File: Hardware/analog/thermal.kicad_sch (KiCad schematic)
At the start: 11 parts, among them M501 Fan_4pin, Q501 MMBT3904, Q502 PN2222A, U501 EMC2101-R

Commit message: More tweaks to load board
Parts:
- added J501, J502: Conn_01x01, programmable-load:MillMax-2108-2, symbol Connector_Generic:Conn_01x01
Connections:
- net TEMP_DN: now also J502.1 (Pin_1)
- net TEMP_DP: now also J501.1 (Pin_1)
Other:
- moved on the sheet: Q502
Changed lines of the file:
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@@
   (junction (at 214.63 102.87) (diameter 0) (color 0 0 0 0)
   )
-  (junction (at 259.08 30.48) (diameter 0) (color 0 0 0 0)
-  )
   (junction (at 228.6 97.79) (diameter 0) (color 0 0 0 0)
   )
+  (junction (at 259.08 27.94) (diameter 0) (color 0 0 0 0)
+  )
   (junction (at 236.22 105.41) (diameter 0) (color 0 0 0 0)
   )
@@
     (stroke (width 0) (type default) (color 0 0 0 0))
   )
+  (wire (pts (xy 259.08 22.86) (xy 259.08 27.94))
+    (stroke (width 0) (type default) (color 0 0 0 0))
+  )
+  (wire (pts (xy 266.7 33.02) (xy 266.7 35.56))
+    (stroke (width 0) (type default) (color 0 0 0 0))
+  )
   (wire (pts (xy 196.85 38.1) (xy 198.12 38.1))
     (stroke (width 0) (type default) (color 0 0 0 0))
@@
     (stroke (width 0) (type default) (color 0 0 0 0))
   )
-  (wire (pts (xy 249.555 30.48) (xy 259.08 30.48))
+  (wire (pts (xy 249.555 27.94) (xy 259.08 27.94))
     (stroke (width 0) (type default) (color 0 0 0 0))
   )
@@
     (stroke (width 0) (type default) (color 0 0 0 0))
   )
-  (wire (pts (xy 259.08 25.4) (xy 259.08 30.48))
-    (stroke (width 0) (type default) (color 0 0 0 0))
-  )
-  (wire (pts (xy 266.7 25.4) (xy 259.08 25.4))
+  (wire (pts (xy 266.7 22.86) (xy 259.08 22.86))
     (stroke (width 0) (type default) (color 0 0 0 0))
   )
@@
   )
   (text "Place Q502 on/near heatsink,\nconnected via twisted pair wire\nUsed for hardware fan control"
-    (at 278.13 42.545 0)
+    (at 272.415 44.45 0)
     (effects (font (size 1.27 1.27)) (justify right bottom))
   )
@@
     (effects (font (size 1.27 1.27)) (justify left bottom))
   )
-  (label "TEMP_DP" (at 249.555 30.48 0)
+  (label "TEMP_DP" (at 249.555 27.94 0)
     (effects (font (size 1.27 1.27)) (justify left bottom))
   )
@@
     (pin "2")
   )
+  (symbol (lib_id "Connector_Generic:Conn_01x01") (at 244.475 27.94 0) (mirror y) (unit 1)
+    (in_bom yes) (on_board yes)
+    (property "Reference" "J501" (id 0) (at 244.475 24.13 0))
+    (property "Value" "Conn_01x01" (id 1) (at 244.475 24.13 0)
+      (effects (font (size 1.27 1.27)) hide)
+    )
+    (property "Footprint" "programmable-load:MillMax-2108-2" (id 2) (at 244.475 27.94 0)
+      (effects (font (size 1.27 1.27)) hide)
+    )
+    (property "Datasheet" "~" (id 3) (at 244.475 27.94 0)
+      (effects (font (size 1.27 1.27)) hide)
+    )
+    (property "MPN" "2108-2-00-01-00-00-07-0" (id 4) (at 244.475 27.94 0)
+      (effects (font (size 1.27 1.27)) hide)
+    )
+    (pin "1")
+  )
   (symbol (lib_id "Device:R_Small") (at 209.55 91.44 0) (mirror x) (unit 1)
     (in_bom yes) (on_board yes) (fields_autoplaced)
@@
     (pin "1")
   )
+  (symbol (lib_id "Connector_Generic:Conn_01x01") (at 244.475 35.56 0) (mirror y) (unit 1)
+    (in_bom yes) (on_board yes)
+    (property "Reference" "J502" (id 0) (at 244.475 31.75 0))
+    (property "Value" "Conn_01x01" (id 1) (at 244.475 31.75 0)
+      (effects (font (size 1.27 1.27)) hide)
+    )
+    (property "Footprint" "programmable-load:MillMax-2108-2" (id 2) (at 244.475 35.56 0)
+      (effects (font (size 1.27 1.27)) hide)
+    )
+    (property "Datasheet" "~" (id 3) (at 244.475 35.56 0)
+      (effects (font (size 1.27 1.27)) hide)
+    )
+    (property "MPN" "2108-2-00-01-00-00-07-0" (id 4) (at 244.475 35.56 0)
+      (effects (font (size 1.27 1.27)) hide)
+    )
+    (pin "1")
+  )
   (symbol (lib_id "Device:C_Polarized_Small") (at 252.73 99.06 0) (unit 1)
     (in_bom yes) (on_board yes) (fields_autoplaced)
@@
     (pin "4")
   )
-  (symbol (lib_id "Transistor_BJT:PN2222A") (at 264.16 30.48 0) (unit 1)
+  (symbol (lib_id "Transistor_BJT:PN2222A") (at 264.16 27.94 0) (unit 1)
     (in_bom yes) (on_board no) (fields_autoplaced)
-    (property "Reference" "Q502" (id 0) (at 269.875 29.2099 0)
-      (effects (font (size 1.27 1.27)) (justify left))
-    )
-    (property "Value" "PN2222A" (id 1) (at 269.875 31.7499 0)
-      (effects (font (size 1.27 1.27)) (justify left))
-    )
-    (property "Footprint" "Package_TO_SOT_THT:TO-92_Inline" (id 2) (at 269.24 32.385 0)
+    (property "Reference" "Q502" (id 0) (at 269.875 26.6699 0)
+      (effects (font (size 1.27 1.27)) (justify left))
+    )
+    (property "Value" "PN2222A" (id 1) (at 269.875 29.2099 0)
+      (effects (font (size 1.27 1.27)) (justify left))
+    )
+    (property "Footprint" "Package_TO_SOT_THT:TO-92_Inline" (id 2) (at 269.24 29.845 0)
       (effects (font (size 1.27 1.27) italic) (justify left) hide)
     )
-    (property "Datasheet" "https://www.onsemi.com/pub/Collateral/PN2222-D.PDF" (id 3) (at 264.16 30.48 0)
+    (property "Datasheet" "https://www.onsemi.com/pub/Collateral/PN2222-D.PDF" (id 3) (at 264.16 27.94 0)
       (effects (font (size 1.27 1.27)) (justify left) hide)
     )
-    (property "MPN" "PN2222ATA" (id 4) (at 264.16 30.48 0)
-      (effects (font (size 1.27 1.27)) hide)
-    )
+    (property "MPN" "PN2222ATA" (id 4) (at 264.16 27.94 0)
+      (effects (font (size 1.27 1.27)) hide)
+    )

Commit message: Initial pass at analog board
- Everything currently in the schematic is routed, and stuff is
  reasonably sanely laid out

- Some compromises: namely, the zero offset doesn't use the DAC
  reference for its positive, but generates a separate 2.5V via the
  shunt diodes; this is then shared between both op-amps. That avoids
  the DAC/ADC reference getting noisified

  Also, we don't have an ADC for measuring the temperature sensors yet,
  and in fact, those aren't routed out (or existent really) yet either

- TODO: add test points for drive voltages and current sense voltages
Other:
- title: (none) -> 300W Analog Load Board
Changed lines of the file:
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@@
 (kicad_sch (version 20211123) (generator eeschema)
   (paper "A4")
+  (title_block
+    (title "300W Analog Load Board")
+    (rev "1")
+  )
   (junction (at 214.63 102.87) (diameter 0) (color 0 0 0 0)
   )

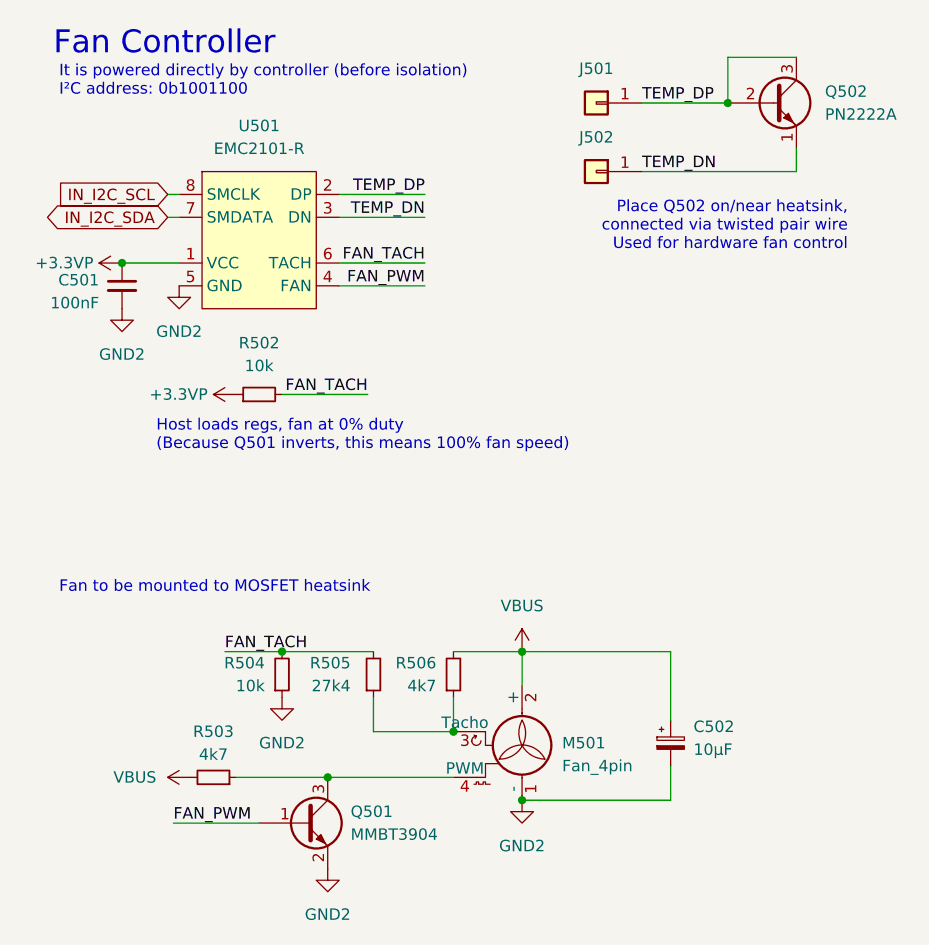
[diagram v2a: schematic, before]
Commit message: Added more decoupling for reference
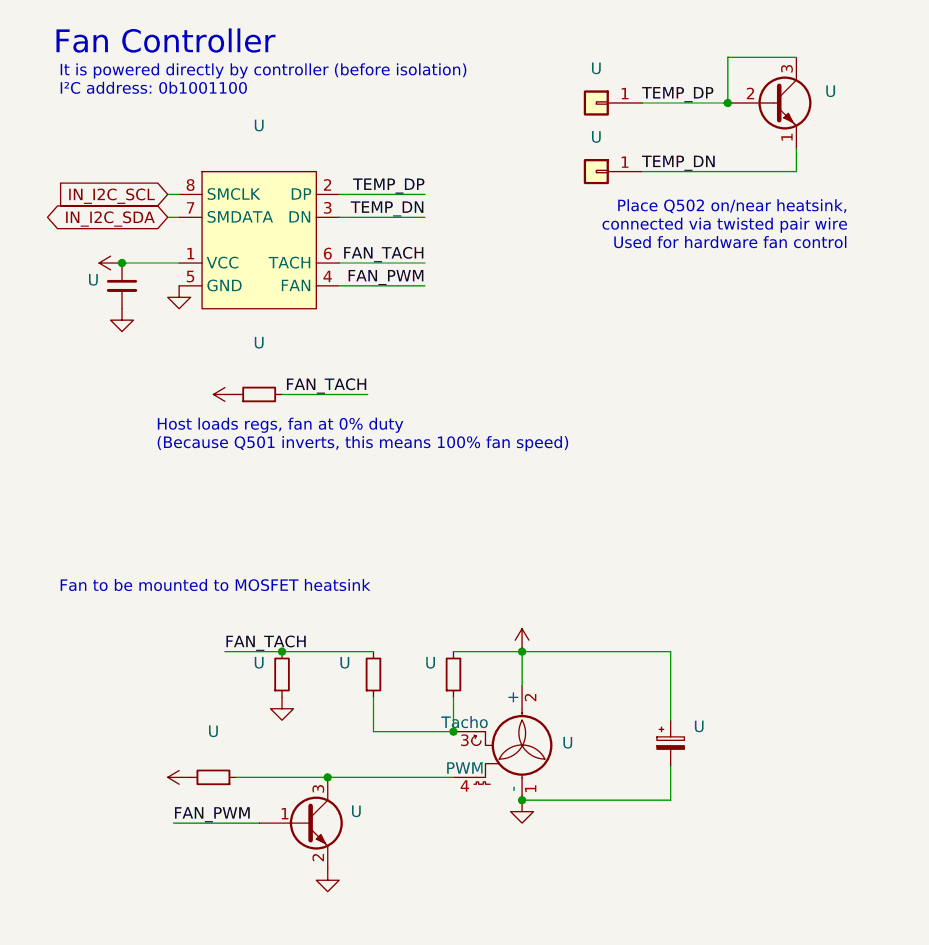
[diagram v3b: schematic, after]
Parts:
- U: renamed from U501; value EMC2101-R -> (none); footprint Package_SO:MSOP-8_3x3mm_P0.65mm -> (none)
- U: renamed from R506; value 4k7 -> (none); footprint Resistor_SMD:R_0805_2012Metric_Pad1.20x1.40mm_HandSolder -> (none)
- U: renamed from J501; value Conn_01x01 -> (none); footprint programmable-load:MillMax-2108-2 -> (none)
- U: renamed from R504; value 10k -> (none); footprint Resistor_SMD:R_0805_2012Metric_Pad1.20x1.40mm_HandSolder -> (none)
- U: renamed from C501; value 100nF -> (none); footprint Capacitor_SMD:C_0805_2012Metric_Pad1.18x1.45mm_HandSolder -> (none)
- U: renamed from R502; value 10k -> (none); footprint Resistor_SMD:R_0805_2012Metric_Pad1.20x1.40mm_HandSolder -> (none)
- U: renamed from J502; value Conn_01x01 -> (none); footprint programmable-load:MillMax-2108-2 -> (none)
- U: renamed from C502; value 10µF -> (none); footprint Capacitor_THT:CP_Radial_D5.0mm_P2.00mm -> (none)
- U: renamed from Q501; value MMBT3904 -> (none); footprint Package_TO_SOT_SMD:SOT-323_SC-70_Handsoldering -> (none)
- U: renamed from M501; value Fan_4pin -> (none); footprint programmable-load:Molex-47053-1000-MFG -> (none)
- U: renamed from Q502; value PN2222A -> (none); footprint Package_TO_SOT_THT:TO-92_Inline -> (none)
- U: renamed from R503; value 4k7 -> (none); footprint Resistor_SMD:R_0805_2012Metric_Pad1.20x1.40mm_HandSolder -> (none)
- U: renamed from R505; value 27k4 -> (none); footprint Resistor_SMD:R_0805_2012Metric_Pad1.20x1.40mm_HandSolder -> (none)

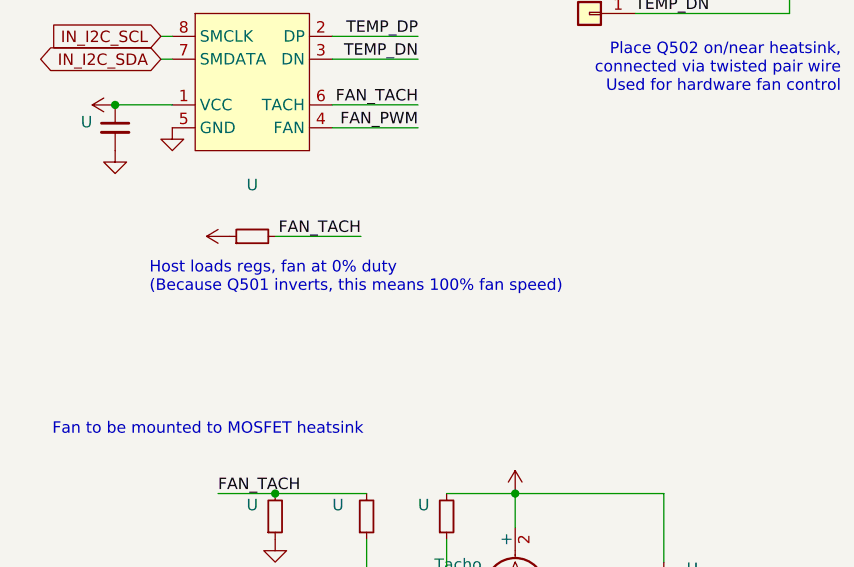
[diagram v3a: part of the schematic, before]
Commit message: Analog board tweaks
- Moved a few traces and components around to accomodate other changes
  in the controller stuff, preparation for some sort of cleanup

- Aesthetic moves of labels on controller board
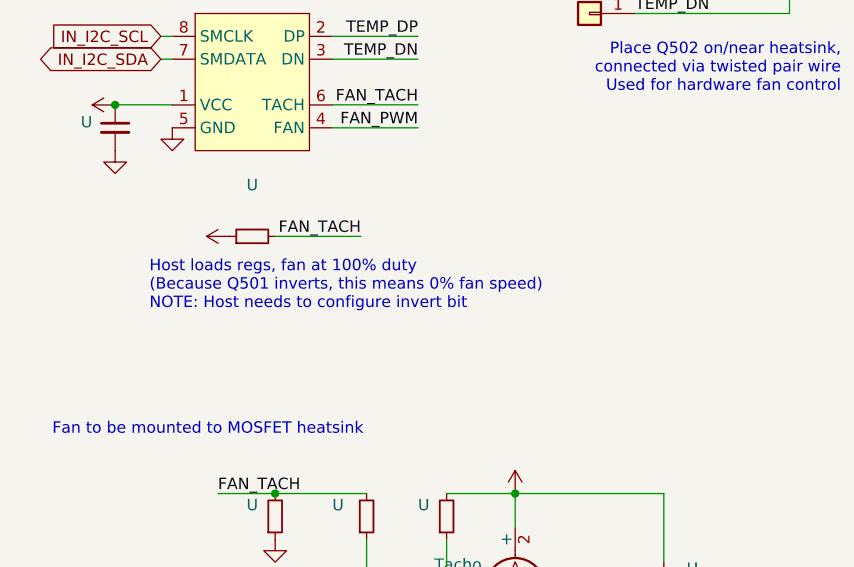
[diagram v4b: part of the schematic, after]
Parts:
- U: MPN RMC1/10-103JTP -> (none)
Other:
- note added: "Host loads regs, fan at 100% duty (Because Q501 inverts, this means 0% fan speed) NOTE: Host needs to configure invert bit"
- note removed: "Host loads regs, fan at 0% duty (Because Q501 inverts, this means 100% fan speed)"
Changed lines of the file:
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@@
     (effects (font (size 2.54 2.54)) (justify left bottom))
   )
-  (text "Host loads regs, fan at 0% duty\n(Because Q501 inverts, this means 100% fan speed)"
-    (at 195.58 66.675 0)
+  (text "Host loads regs, fan at 100% duty\n(Because Q501 inverts, this means 0% fan speed)\nNOTE: Host needs to configure invert bit"
+    (at 195.58 68.58 0)
     (effects (font (size 1.27 1.27)) (justify left bottom))
   )
@@
       (effects (font (size 1.27 1.27)) hide)
     )
-    (property "MPN" "RMC1/10-103JTP" (id 4) (at 207.01 60.325 90)
-      (effects (font (size 1.27 1.27)) hide)
-    )
+    (property "MPN" "" (id 4) (at 207.01 60.325 90)
+      (effects (font (size 1.27 1.27)) hide)
+    )

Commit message: Mostly finished up analog load board
- Finished routing most signals

- Connected relay drive to bonus I2C GPIO controller, and routed the
  rest of the voltage sense stuff

- Routed the reset signal to the DAC, so that when the board is reset,
  the current output will be reset to zero as well without processor
  intervention

- Replaced most passives with 0603/1608 size
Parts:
- U: MPN RMC1/10-103JTP -> (none)
- U: MPN 860010472002 -> A768EB336M1GLAE045
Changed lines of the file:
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@@
       (effects (font (size 1.27 1.27)) hide)
     )
-    (property "MPN" "RMC1/10-103JTP" (id 4) (at 209.55 91.44 0)
+    (property "MPN" "" (id 4) (at 209.55 91.44 0)
       (effects (font (size 1.27 1.27)) hide)
     )
@@
       (effects (font (size 1.27 1.27)) hide)
     )
-    (property "MPN" "860010472002" (id 4) (at 252.73 99.06 0)
+    (property "MPN" "A768EB336M1GLAE045" (id 4) (at 252.73 99.06 0)
       (effects (font (size 1.27 1.27)) hide)
     )
